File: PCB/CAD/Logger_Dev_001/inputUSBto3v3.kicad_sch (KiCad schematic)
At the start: 20 parts, among them J4 Connector, USB-TYPE-C-16P, U4 MCP2221AxSL, U6 XC6206P332MR

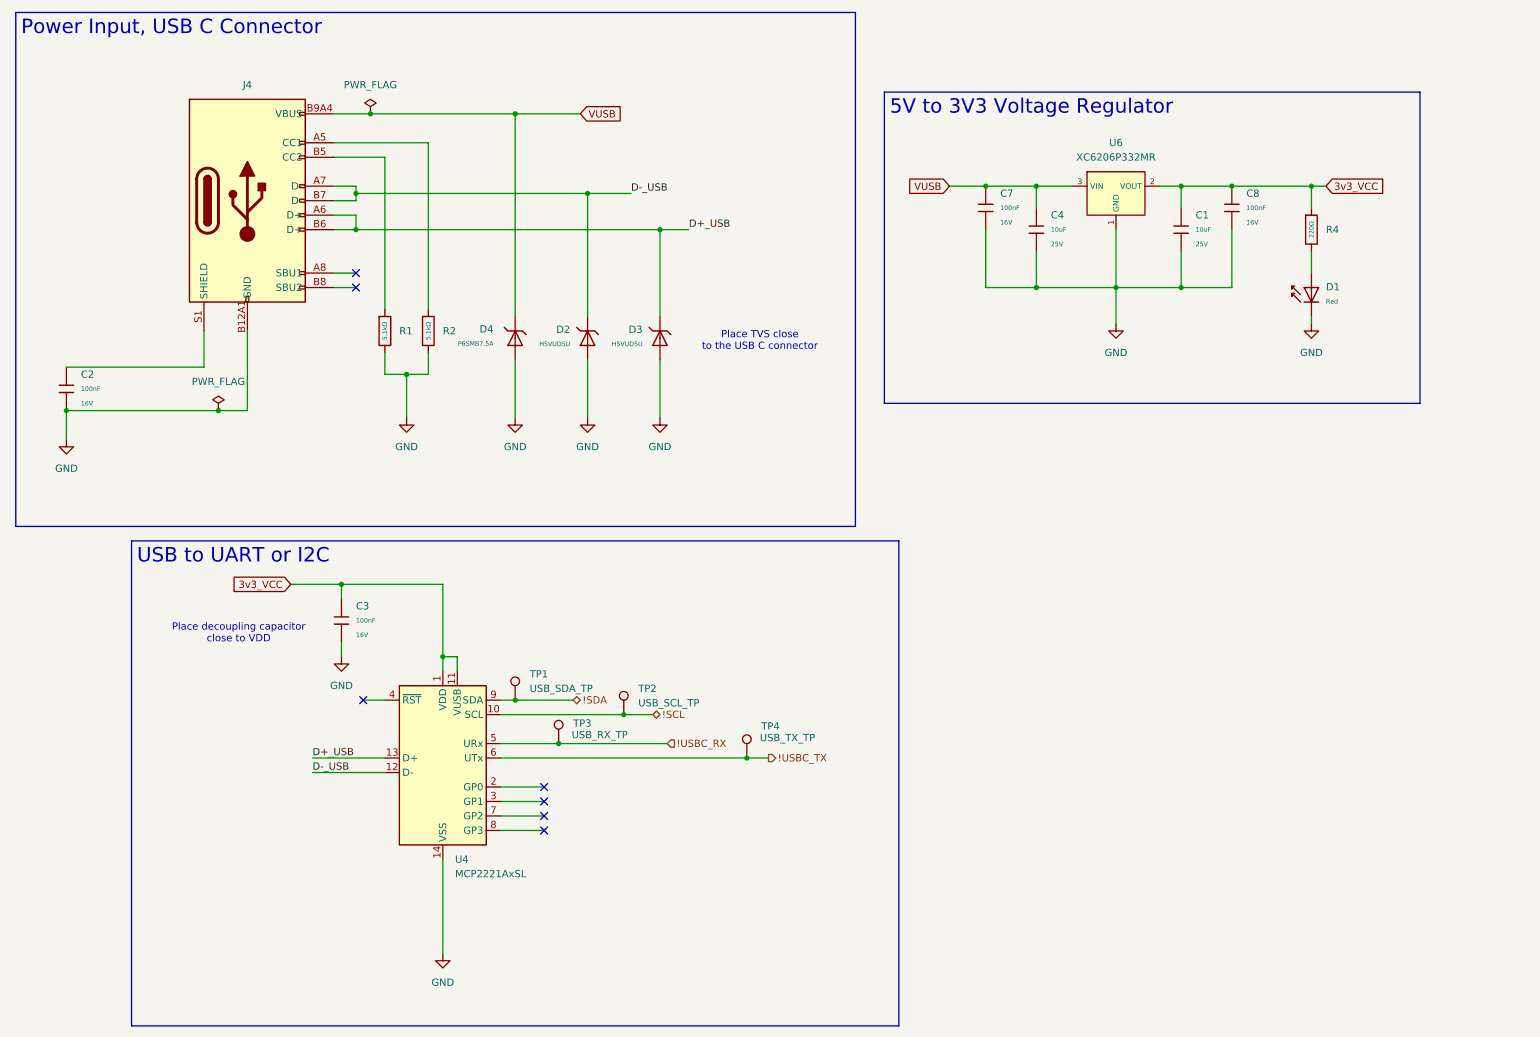
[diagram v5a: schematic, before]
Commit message: USB Schematic update
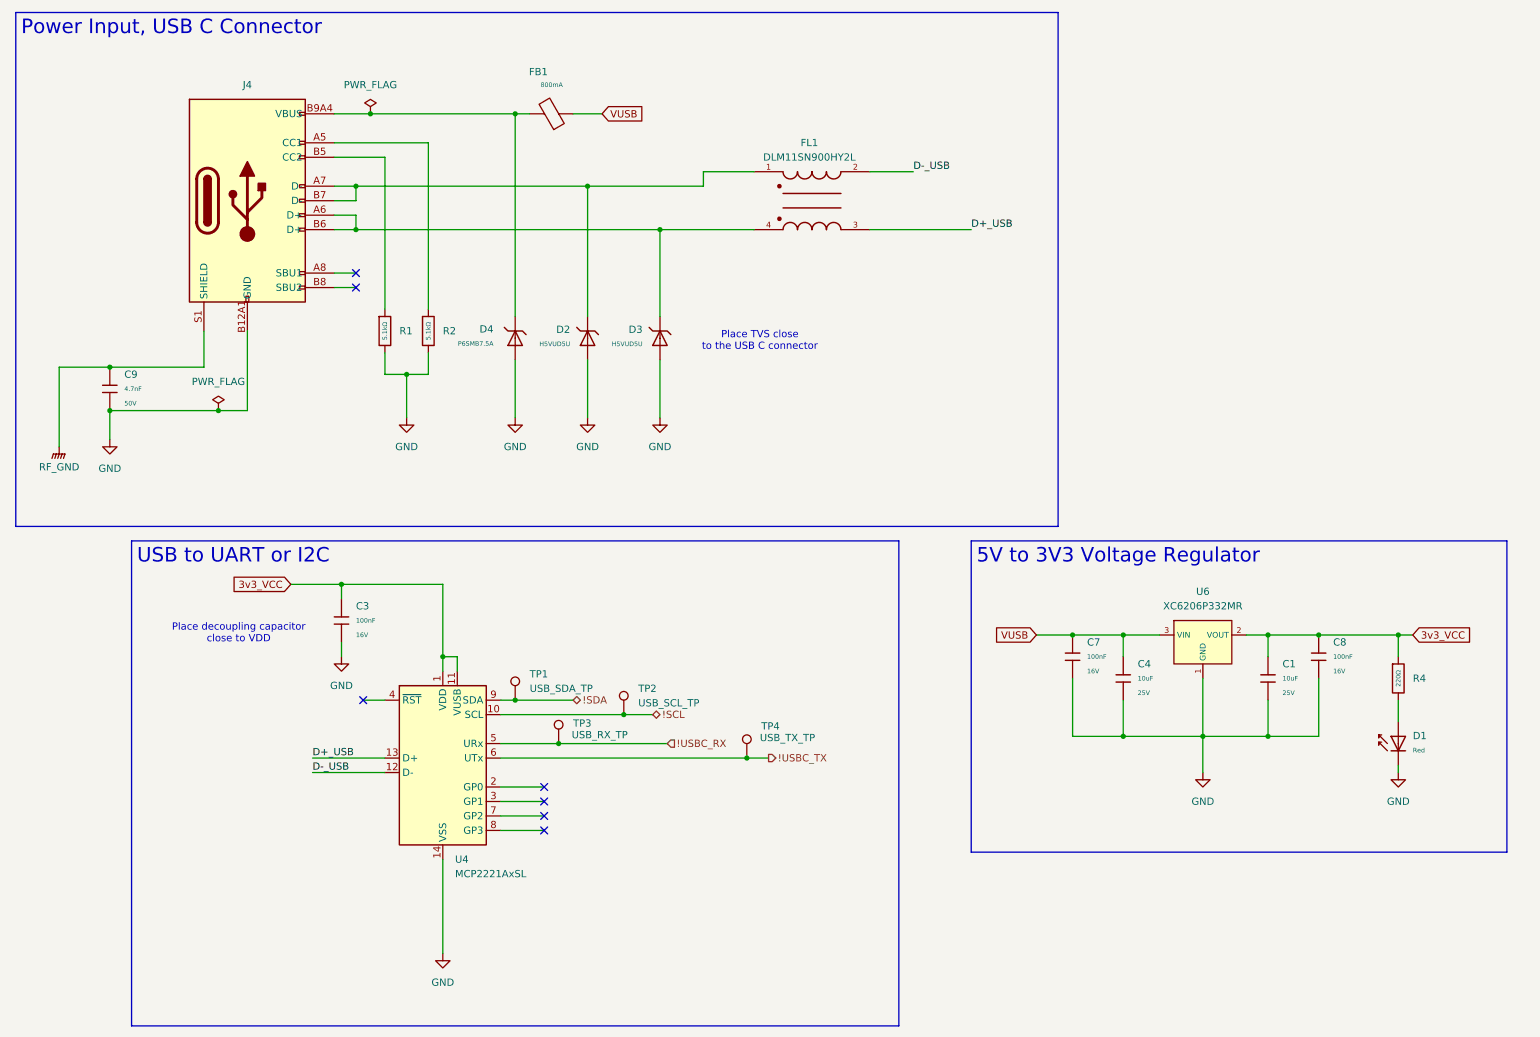
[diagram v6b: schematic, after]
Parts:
- removed C2: 100nF, PCM_JLCPCB:C_0402, symbol PCM_JLCPCB-Capacitors:0402,100nF
- added C9: 4.7nF, PCM_JLCPCB:C_0402, symbol PCM_JLCPCB-Capacitors:0402,4.7nF
- added FB1: ~, PCM_JLCPCB:FB_0805, symbol PCM_JLCPCB-Inductors:Ferrite,0805
- added FL1: DLM11SN900HY2L, DLM11SN900HY2L:FIL_DLM11SN900HY2L, symbol DLM11SN900HY2L:DLM11SN900HY2L
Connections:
- net D+_USB: now also FL1.3; no longer D3.1, J4.A6 (D+), J4.B6 (D+)
- net D-_USB: now also FL1.2; no longer D2.1, J4.A7 (D-), J4.B7 (D-)
- net GND: now also C9.2
- net VUSB: now also FB1.1; no longer D4.1, J4.A9B4 (VBUS), J4.B9A4 (VBUS)
- net RF_GND: now reaches J4.S1 (SHIELD)
- net RF_GND: now also C9.1
- new net: D3.1, FL1.4, J4.A6 (D+), J4.B6 (D+)
- new net: D4.1, FB1.2, J4.A9B4 (VBUS), J4.B9A4 (VBUS)
- new net: D2.1, FL1.1, J4.A7 (D-), J4.B7 (D-)
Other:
- moved on the sheet: C1, C4, C7, C8, D1, R4, U6

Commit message: Updated Schematic
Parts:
- removed U4: MCP2221AxSL, Package_SO:SOIC-14_3.9x8.7mm_P1.27mm, symbol Interface_USB:MCP2221AxSL
- removed U6: XC6206P332MR, PCM_JLCPCB:SOT-23-3_L2.9-W1.6-P1.90-LS2.8-BR, symbol PCM_JLCPCB-Power:LDO, 3.3V, 0.2A
- added C2: 10uF, PCM_JLCPCB:C_0603, symbol PCM_JLCPCB-Capacitors:0603,10uF,(2)
- added Q1: BC847BS, PCM_JLCPCB:SOT-363_SC-70-6, symbol PCM_JLCPCB-Transistor-Packages:NPN, 2 Channel, BC847BS
- added R10, R11, R12: 10kΩ, PCM_JLCPCB:R_0402, symbol PCM_JLCPCB-Resistors:0402,10kΩ
- added R13: 22kΩ, PCM_JLCPCB:R_0402, symbol PCM_JLCPCB-Resistors:0402,22kΩ
- added R14: 47kΩ, PCM_JLCPCB:R_0402, symbol PCM_JLCPCB-Resistors:0402,47kΩ
- added R9: 0Ω, PCM_JLCPCB:R_1206, symbol PCM_JLCPCB-Resistors:1206,0Ω
- added TP5: USB_D+_TP, symbol Connector:TestPoint
- added TP6: USB_D-_TP, symbol Connector:TestPoint
- added U5: AMS1117, PCM_JLCPCB:SOT-223-3_L6.5-W3.4-P2.30-LS7.0-BR, symbol PCM_JLCPCB-Power:LDO, 3.3V, 1A
- added U6: CP2102-GMR, PCM_JLCPCB:WQFN-28_L5.0-W5.0-P0.50-BL-EP3.2, symbol PCM_JLCPCB-Interface:Transceiver, USB
- TP1: value USB_SDA_TP -> DTR
- TP2: value USB_SCL_TP -> RTS
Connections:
- net !USBC_RX: now also TP4.1, U6.25 (RXD); no longer TP3.1
- net !USBC_TX: now also TP3.1, U6.26 (TXD); no longer TP4.1
- net 3v3_VCC: now also R12.1, R9.2, U6.6 (VDD), U6.7 (REGIN); no longer C1.1, C8.1, R4.1
- net D+_USB: now also TP5.1, U6.4 (D+)
- net D-_USB: now also TP6.1, U6.5 (D-)
- net GND: now also C2.2, R14.2, U5.1 (GND), U6.29 (EP), U6.3 (GND)
- net VUSB: now also C2.1, R13.1, U5.3 (VIN)
- net !SCL renamed RTS
- net RTS: now also Q1.4 (E2), R10.1, U6.24 (RTS)
- net !SDA renamed DTR
- net DTR: now also Q1.1 (E1), R11.1, U6.28 (DTR)
- new net: C1.1, C8.1, R4.1, R9.1, U5.2 (VOUT), U5.4 (VOUT)
- new net: Q1.2 (B1), R10.2
- new net: R12.2, U6.9 (RST#)
- new net: R13.2, R14.1, U6.8 (VBUS)
- new net: Q1.5 (B2), R11.2
- new net !EN: Q1.3 (C2)
- new net !GPIO9_BOOT: Q1.6 (C1)
- no-connect marks 7 -> 19
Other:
- note added: "1A Output with 1.8V Dropout Voltage"
- note added: "72% Efficency, Worst Case"
- note added: "Auto program DTR RTS --> EN IO9 1 1 1 1 0 0 1 1 1 0 0 1 0 1 1 0"
- note added: "Place TVS close to the USB C connector for ESD protection"
- note added: "Place bulk capacitor close to USB C connector"
- note removed: "Place TVS close to the USB C connector"
- company: (none) -> Jake Odgers
- title: (none) -> Mileage Logger
- moved on the sheet: C1, C3, C4, C7, C8, C9, D1, D2, D3, D4, FB1, FL1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
